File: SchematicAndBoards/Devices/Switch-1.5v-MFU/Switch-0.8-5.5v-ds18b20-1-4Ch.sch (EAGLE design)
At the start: 18 parts

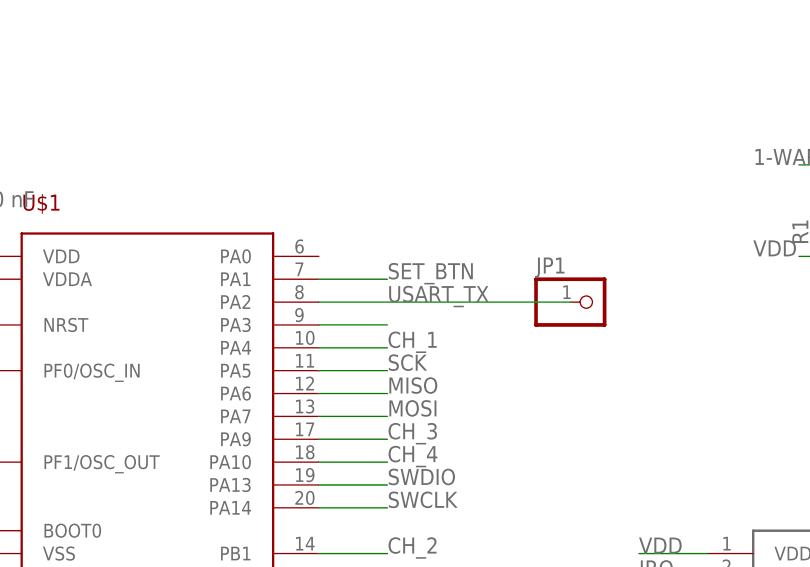
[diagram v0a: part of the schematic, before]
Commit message: Add Eagle boad and schematic for device Switch-1Ware-4Ch-CC1101-F030F4
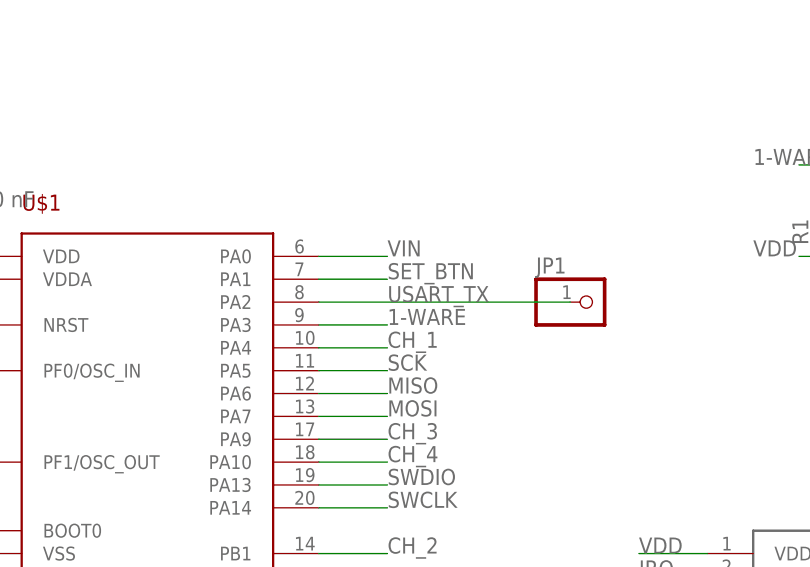
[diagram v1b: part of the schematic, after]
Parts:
- U$2: value TPS6122 -> TPS61221
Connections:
- net VIN: now also U$1.PA0
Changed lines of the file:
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@@
 <part name="CH-OUT" library="pinhead" deviceset="PINHD-1X4" device="_2.54"/>
 <part name="R1" library="resistor" deviceset="R-EU_" device="R0805"/>
-<part name="U$2" library="my_components" deviceset="TPS6122" device=""/>
+<part name="U$2" library="my_components" deviceset="TPS6122" device="" value="TPS61221"/>
 <part name="L2" library="SparkFun-Passives" deviceset="INDUCTOR" device="1210"/>
 <part name="U$3" library="RemoteSwitchComponents" deviceset="AS07-M1101S" device="" value="AS07-M1101S"/>
@@
 <wire x1="-5.08" y1="142.24" x2="-5.08" y2="124.46" width="0.1524" layer="91"/>
 </segment>
+<segment>
+<pinref part="U$1" gate="G$1" pin="PA0"/>
+<wire x1="78.74" y1="60.96" x2="86.36" y2="60.96" width="0.1524" layer="91"/>
+<label x="86.36" y="60.96" size="1.778" layer="95"/>
+</segment>
 </net>
 <net name="1-WARE" class="0">
@@
 <pinref part="U$1" gate="G$1" pin="PA3"/>
 <wire x1="78.74" y1="53.34" x2="86.36" y2="53.34" width="0.1524" layer="91"/>
-</segment>
-</net>
+<label x="86.36" y="53.34" size="1.778" layer="95"/>
+</segment>
+</net>
